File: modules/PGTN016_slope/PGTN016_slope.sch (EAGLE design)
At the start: 124 parts, among them IC1 LM3900N, IC2 TL074P, IC3 TL074P, Q1 2N3906, Q2 2N3904, Q3 2N3904, Q4 2N3906, Q5 2N3906, Q6 2N3904

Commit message: Added files
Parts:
- added LED+: HEADER/MALE/01, connectors:HEADER/MALE/01
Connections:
- net +12V: now also LED+.3
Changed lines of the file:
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@@
 <attribute name="SPICEPREFIX" value="X"/>
+</part>
+<part name="LED+" library="connectors" deviceset="HEADER/MALE/01" device="">
+<attribute name="SPICEPREFIX" value="X"/>
+</part>
+<part name="SUPPLY38" library="supply" deviceset="+12V" device="">
+<attribute name="SPICEPREFIX" value="G"/>
 </part>
 </parts>
@@
 <instance part="R62" gate="G$1" x="203.2" y="-200.66" rot="R90"/>
 <instance part="LED-" gate="HEADER" x="205.74" y="-195.58" rot="R180"/>
+<instance part="LED+" gate="HEADER" x="226.06" y="-198.12"/>
+<instance part="SUPPLY38" gate="+12V" x="228.6" y="-195.58"/>
 </instances>
 <busses>
@@
 <pinref part="SUPPLY30" gate="+12V" pin="+12V"/>
 </segment>
+<segment>
+<pinref part="LED+" gate="HEADER" pin="3"/>
+<pinref part="SUPPLY38" gate="+12V" pin="+12V"/>
+</segment>
 </net>

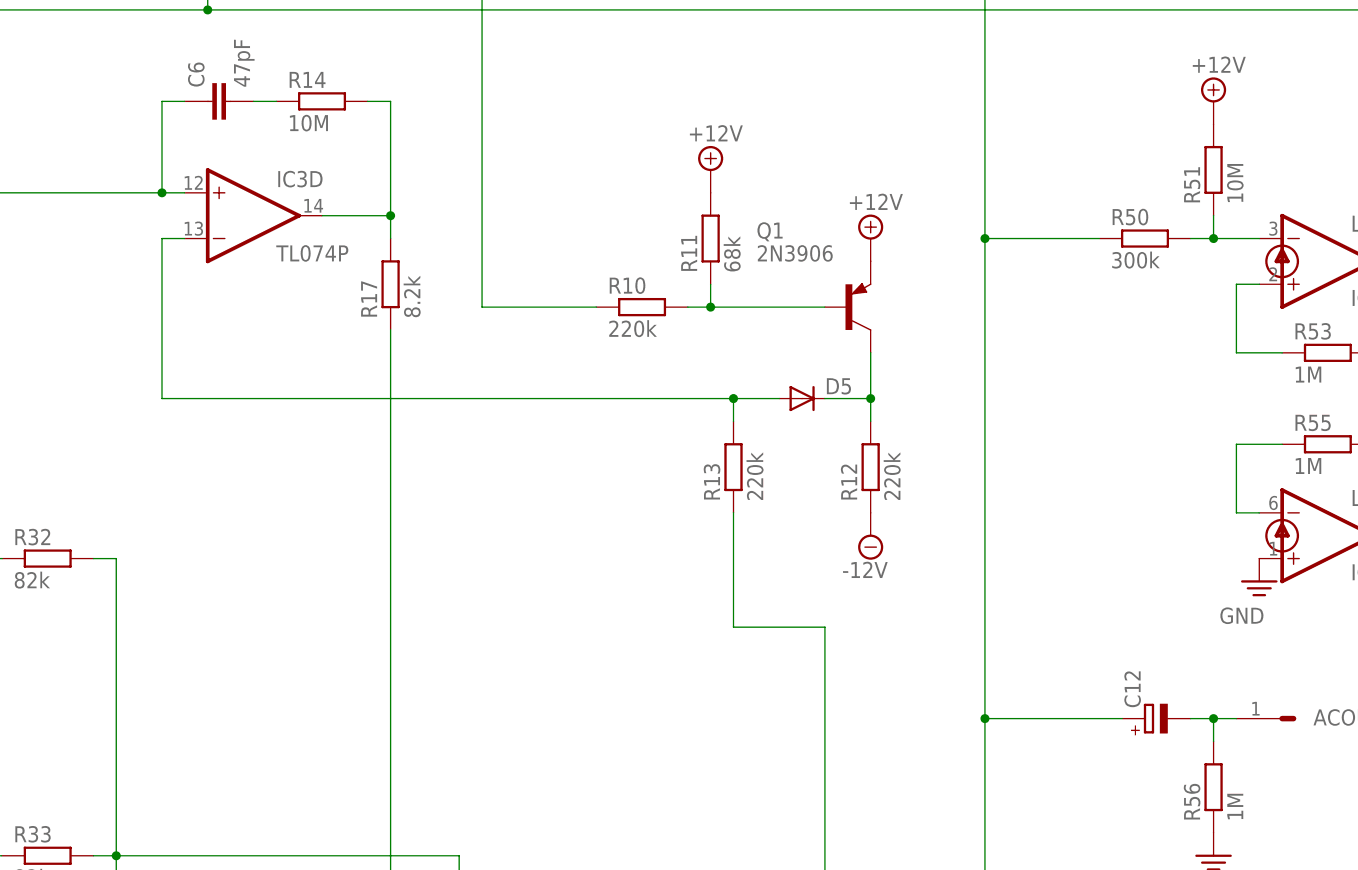
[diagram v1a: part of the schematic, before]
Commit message: PGTN015 V2 - Fix pins 12 and 13 of IC3 (Op amp inputs) wrong way around.
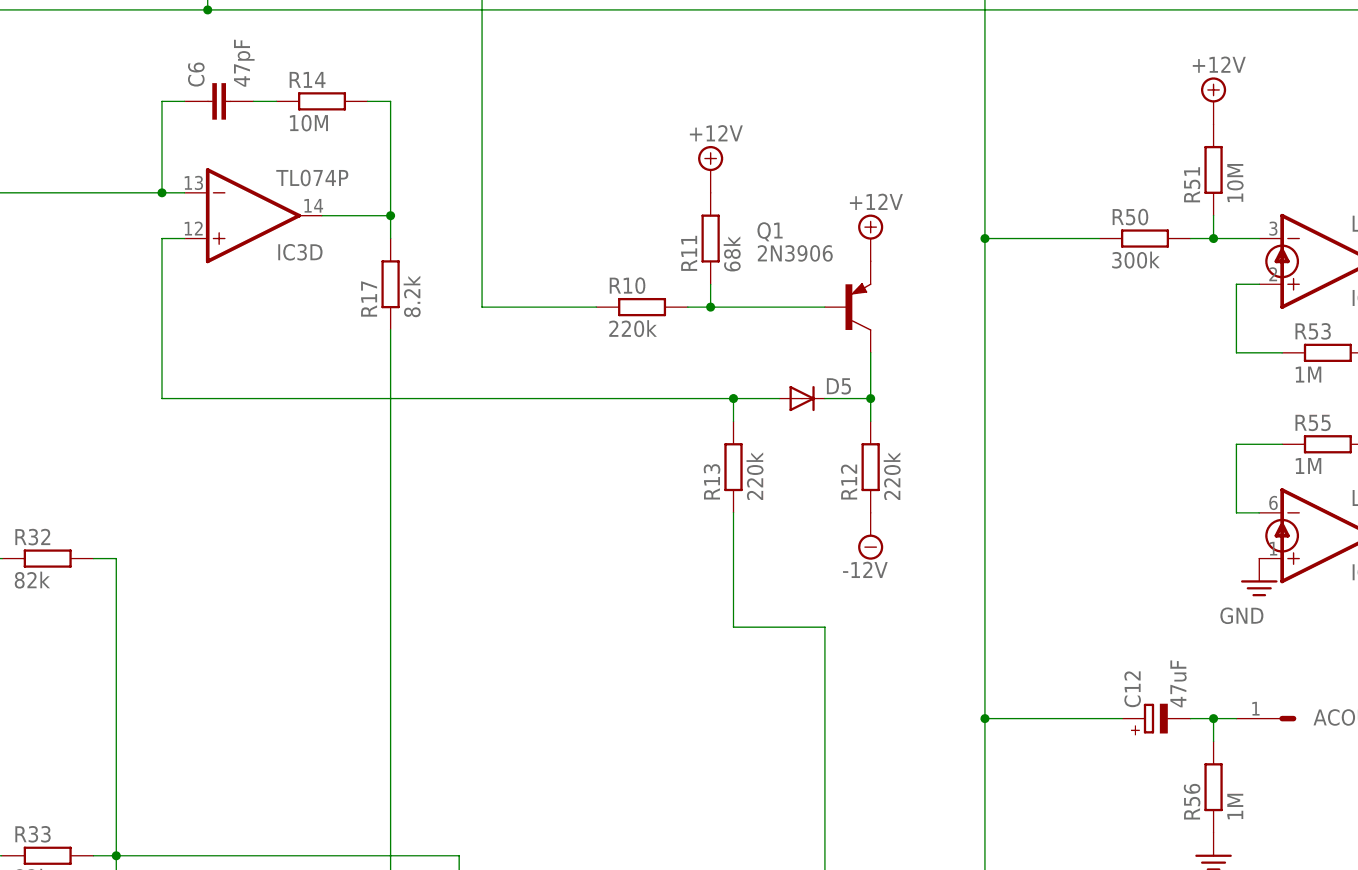
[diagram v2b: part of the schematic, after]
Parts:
- C12: value (none) -> 47uF
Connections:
- net N$16: now also IC3D.+IN; no longer IC3D.-IN
- net N$20: now also IC3D.-IN; no longer IC3D.+IN
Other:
- moved on the sheet: IC3D
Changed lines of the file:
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@@
 <attribute name="SPICEPREFIX" value="G"/>
 </part>
-<part name="C12" library="capacitors" deviceset="CAPACITOR/POLARIZED" device="E2.5-6"/>
+<part name="C12" library="capacitors" deviceset="CAPACITOR/POLARIZED" device="E2.5-6" value="47uF"/>
 <part name="R56" library="resistors" deviceset="RESISTOR" device="RESISTOR/UPRIGHT/7.5" value="1M"/>
 <part name="SUPPLY33" library="supply" deviceset="GND" device="">
@@
 <instance part="IC3" gate="B" x="218.44" y="-165.1" rot="MR180"/>
 <instance part="IC3" gate="C" x="149.86" y="-167.64" rot="MR180"/>
-<instance part="IC3" gate="D" x="99.06" y="-55.88"/>
+<instance part="IC3" gate="D" x="99.06" y="-55.88" rot="MR180"/>
 <instance part="IC2" gate="P" x="48.26" y="53.34"/>
 <instance part="IC3" gate="P" x="55.88" y="53.34"/>
@@
 <wire x1="88.9" y1="-76.2" x2="88.9" y2="-58.42" width="0.1524" layer="91"/>
 <junction x="152.4" y="-76.2"/>
-<pinref part="IC3" gate="D" pin="-IN"/>
+<pinref part="IC3" gate="D" pin="+IN"/>
 <wire x1="91.44" y1="-58.42" x2="88.9" y2="-58.42" width="0.1524" layer="91"/>
 </segment>
@@
 <net name="N$18" class="0">
 <segment>
+<pinref part="R14" gate="G$1" pin="2"/>
 <wire x1="114.3" y1="-58.42" x2="114.3" y2="-55.88" width="0.1524" layer="91"/>
-<pinref part="R14" gate="G$1" pin="2"/>
 <wire x1="114.3" y1="-55.88" x2="114.3" y2="-43.18" width="0.1524" layer="91"/>
 <wire x1="114.3" y1="-43.18" x2="111.76" y2="-43.18" width="0.1524" layer="91"/>
@@
 <pinref part="R15" gate="G$1" pin="2"/>
 <wire x1="-12.7" y1="-53.34" x2="88.9" y2="-53.34" width="0.1524" layer="91"/>
-<pinref part="IC3" gate="D" pin="+IN"/>
-<wire x1="91.44" y1="-53.34" x2="88.9" y2="-53.34" width="0.1524" layer="91"/>
+<pinref part="IC3" gate="D" pin="-IN"/>
+<wire x1="88.9" y1="-53.34" x2="91.44" y2="-53.34" width="0.1524" layer="91"/>
 <junction x="88.9" y="-53.34"/>
 </segment>
